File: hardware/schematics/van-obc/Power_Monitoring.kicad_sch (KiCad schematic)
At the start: 6 parts, among them U3 INA226_12V, U4 INA226_5V

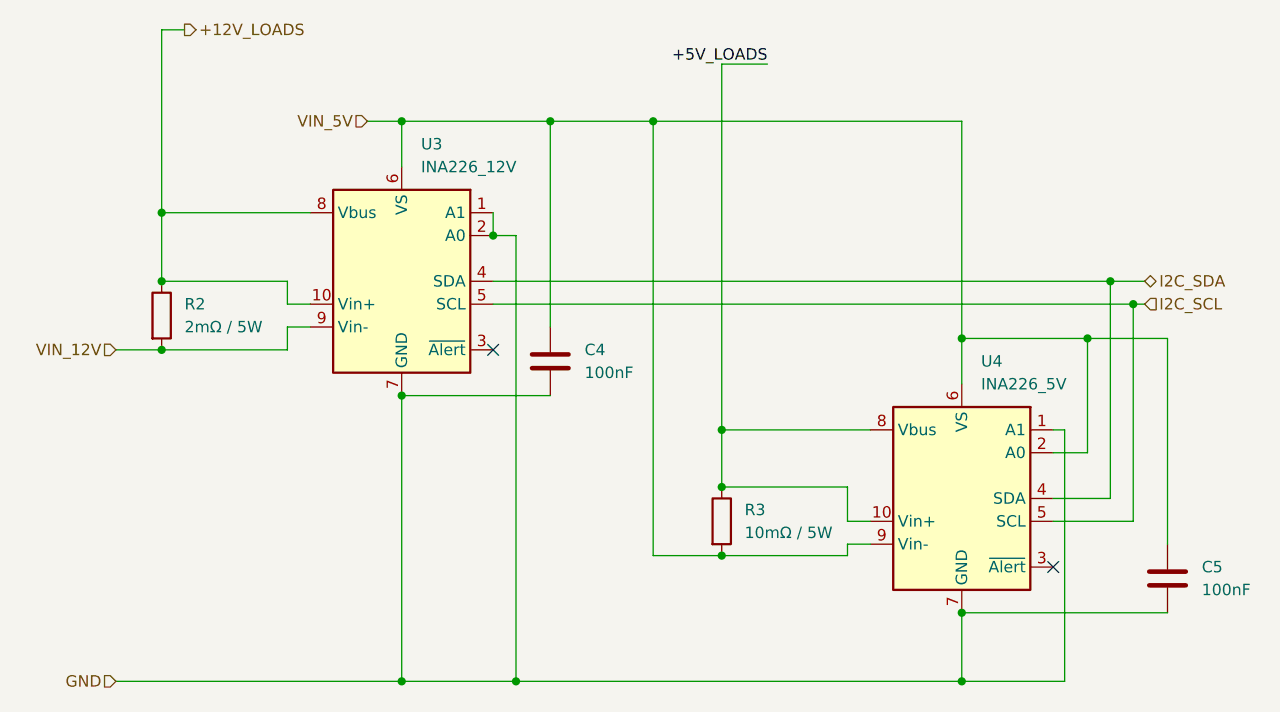
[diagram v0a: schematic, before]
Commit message: fix(tests): Corrections majeures KY040, BME280, MPU6050
- KY040 v2.1.0: Fix comptage + anti-rebond capacitif
- BME280 v1.0.1: Fix begin() avec &Wire
- MPU6050 v2.0.0: Simplification (acc only, dérive <2°)
- Ajout diagnostic_bme280.ino + CHANGELOG

Tests: 6/11 validés (55%)
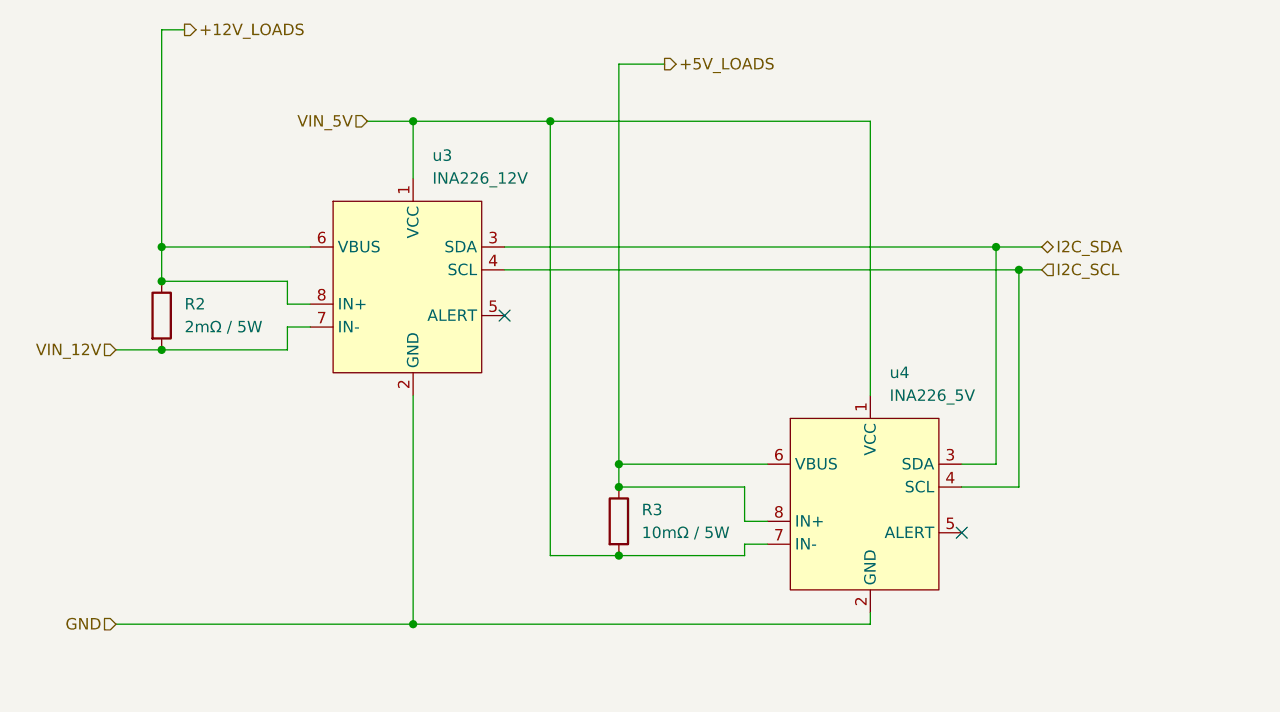
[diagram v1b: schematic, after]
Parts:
- removed C4, C5: 100nF, symbol Device:C
- removed U3: INA226_12V, Package_SO:VSSOP-10_3x3mm_P0.5mm, symbol Sensor_Energy:INA226
- removed U4: INA226_5V, Package_SO:VSSOP-10_3x3mm_P0.5mm, symbol Sensor_Energy:INA226
- added u3: INA226_12V, MyModules:INA226_Module_Header_1x08, symbol MyModules:INA226_Module
- added u4: INA226_5V, MyModules:INA226_Module_Header_1x08, symbol MyModules:INA226_Module
- R2, R3: footprint (none) -> Resistor_SMD:R_2512_6332Metric
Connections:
- net +12V_LOADS: now also u3.6 (VBUS), u3.8 (IN+)
- net +5V_LOADS: now also u4.6 (VBUS), u4.8 (IN+)
- net GND: now also u3.2 (GND), u4.2 (GND)
- net I2C_SCL: now also u3.4 (SCL), u4.4 (SCL)
- net I2C_SDA: now also u3.3 (SDA), u4.3 (SDA)
- net VIN_12V: now also u3.7 (IN-)
- net VIN_5V: now also u3.1 (VCC), u4.1 (VCC), u4.7 (IN-)
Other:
- moved on the sheet: R3
